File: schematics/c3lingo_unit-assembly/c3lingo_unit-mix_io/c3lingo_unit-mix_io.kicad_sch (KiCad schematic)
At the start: 45 parts, among them J201 Stage Line-In, J202 Mix Line-Out, J203 PowerSupply, J204 Ch1, J205 Ch2, J206 Ch3, SW201 GND Lift, U201 LM833-N, U202 DRV135UA, U203 LM833-N

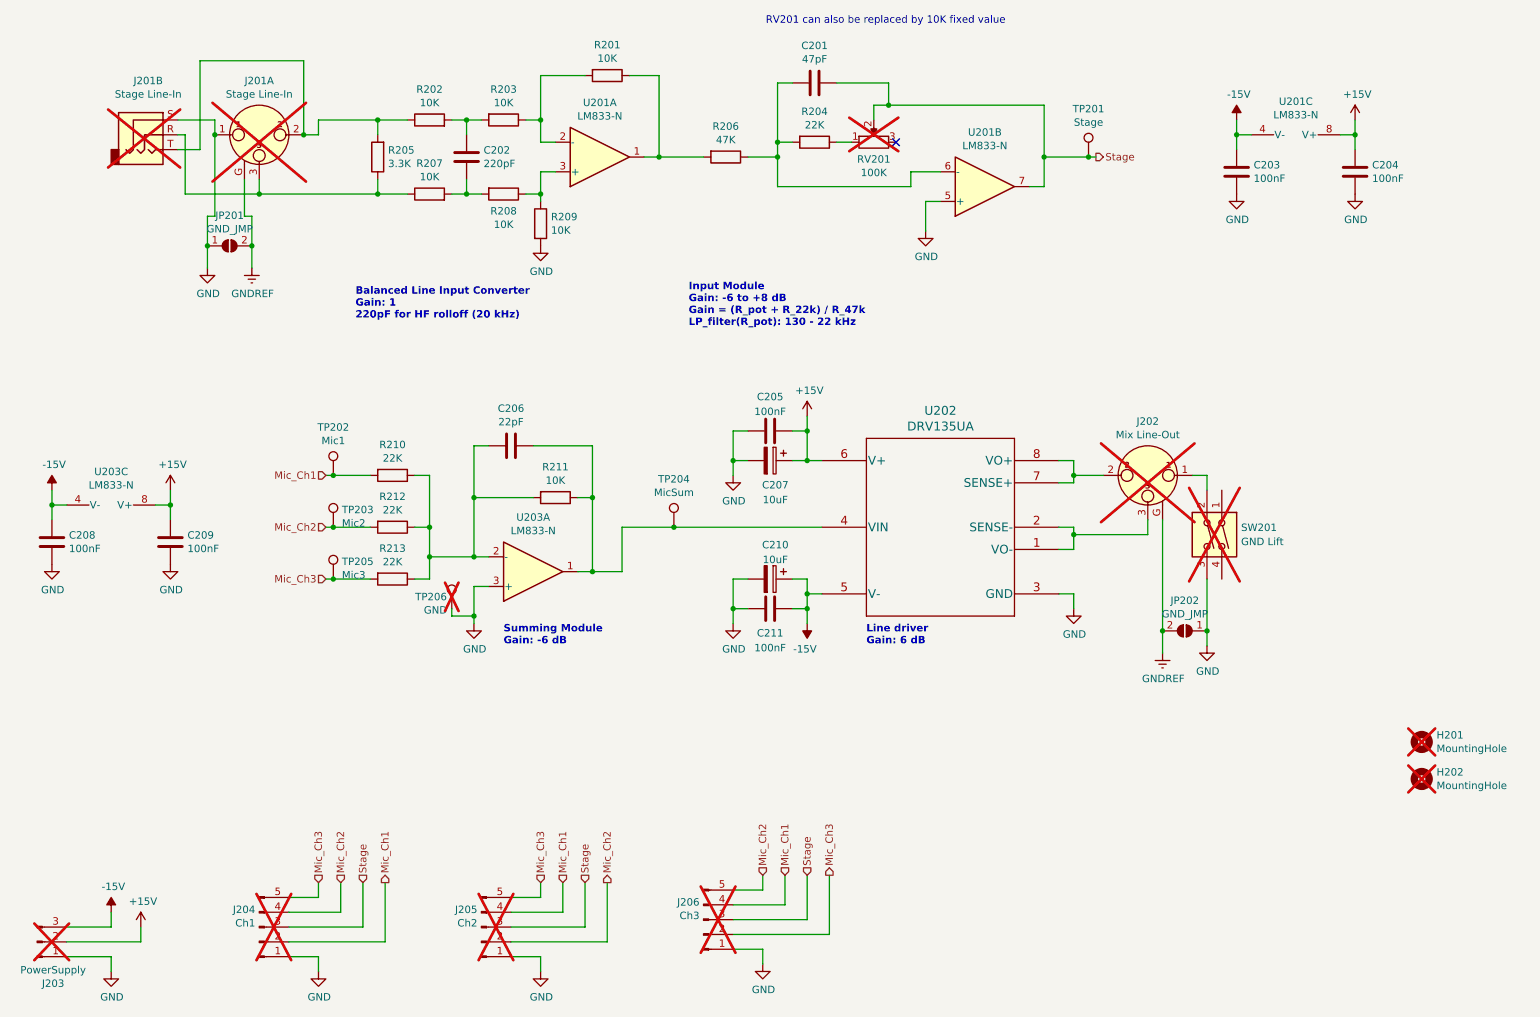
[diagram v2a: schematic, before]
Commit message: Line I/O: Remove gain adjustment (PCB not updated!)
Tweaking the line input gain is not necessary as the users will adjust the volume to personal preference anyways.

Note: PCB not updated!
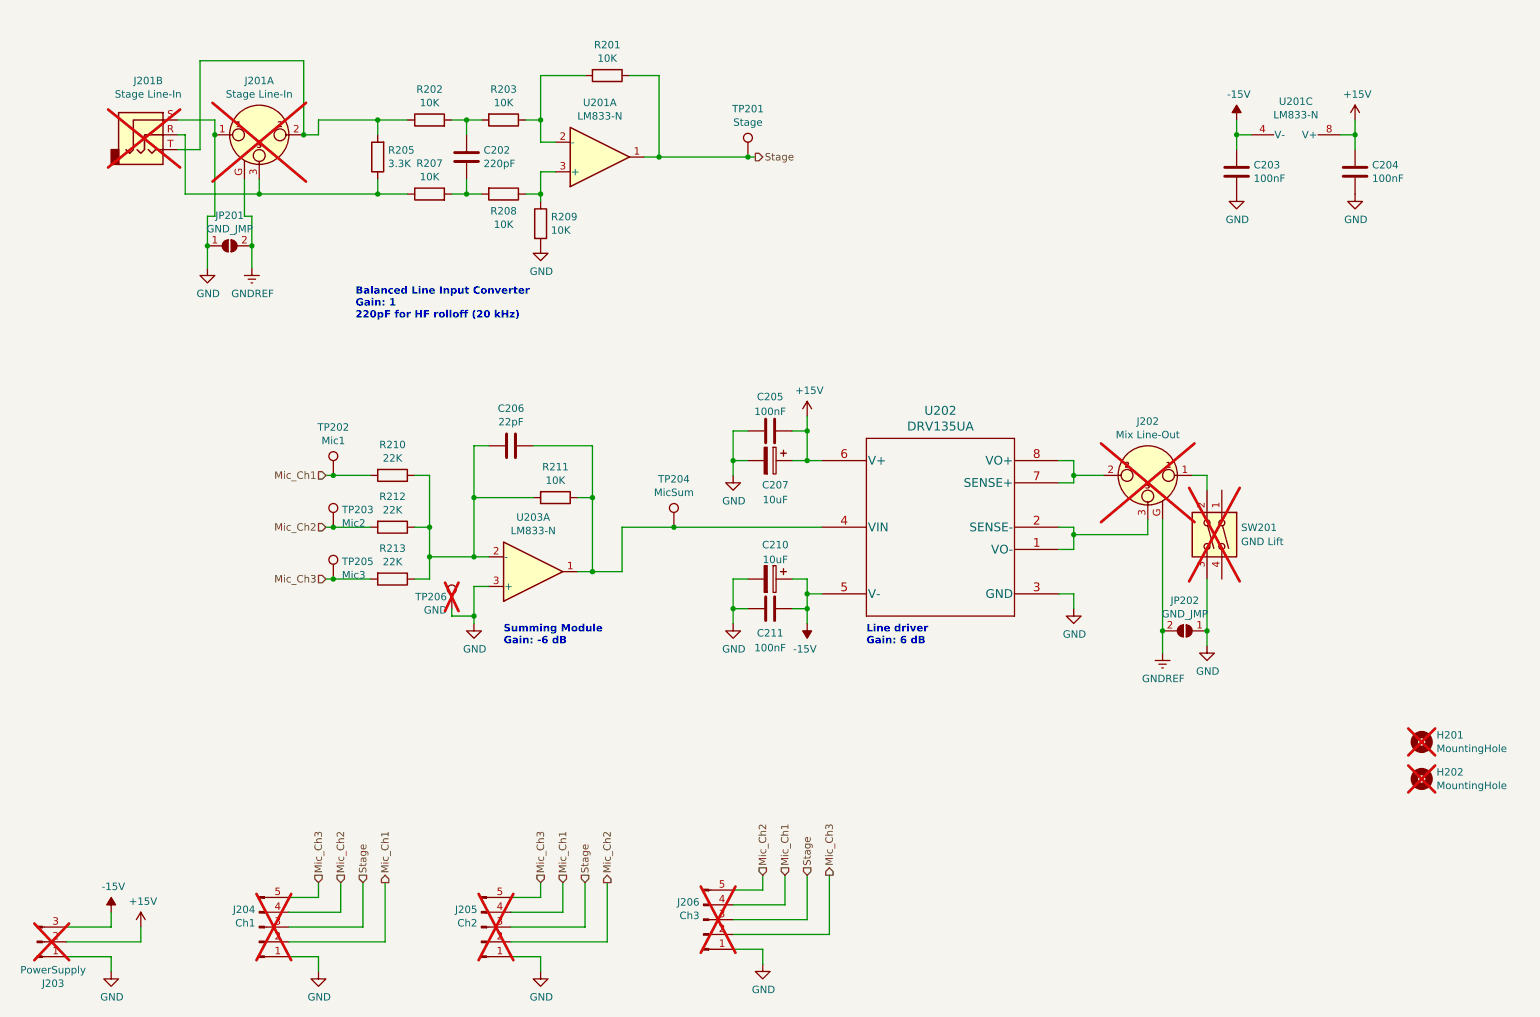
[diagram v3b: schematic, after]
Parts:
- removed C201: 47pF, Capacitor_SMD:C_0603_1608Metric_Pad1.08x0.95mm_HandSolder, symbol Device:C
- removed C208, C209: 100nF, Capacitor_SMD:C_0603_1608Metric_Pad1.08x0.95mm_HandSolder, symbol Device:C
- removed R204: 22K, Resistor_SMD:R_0805_2012Metric_Pad1.20x1.40mm_HandSolder, symbol Device:R
- removed R206: 47K, Resistor_SMD:R_0805_2012Metric_Pad1.20x1.40mm_HandSolder, symbol Device:R
- removed RV201: 100K, Potentiometer_THT:Potentiometer_Vishay_T73XX_Horizontal, symbol Device:R_Potentiometer
- removed unit 2 of U201
- removed unit 3 of U203
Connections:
- net Stage: now also R201.1, U201.1
- no-connect marks 1 -> 0
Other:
- note removed: "Input Module Gain: -6 to +8 dB Gain = (R_pot + R_22k) / R_47k LP_filter(R_pot): 130 - 22 kHz"
- note removed: "RV201 can also be replaced by 10K fixed value"
- moved on the sheet: TP201

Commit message: Update to KiCad 9
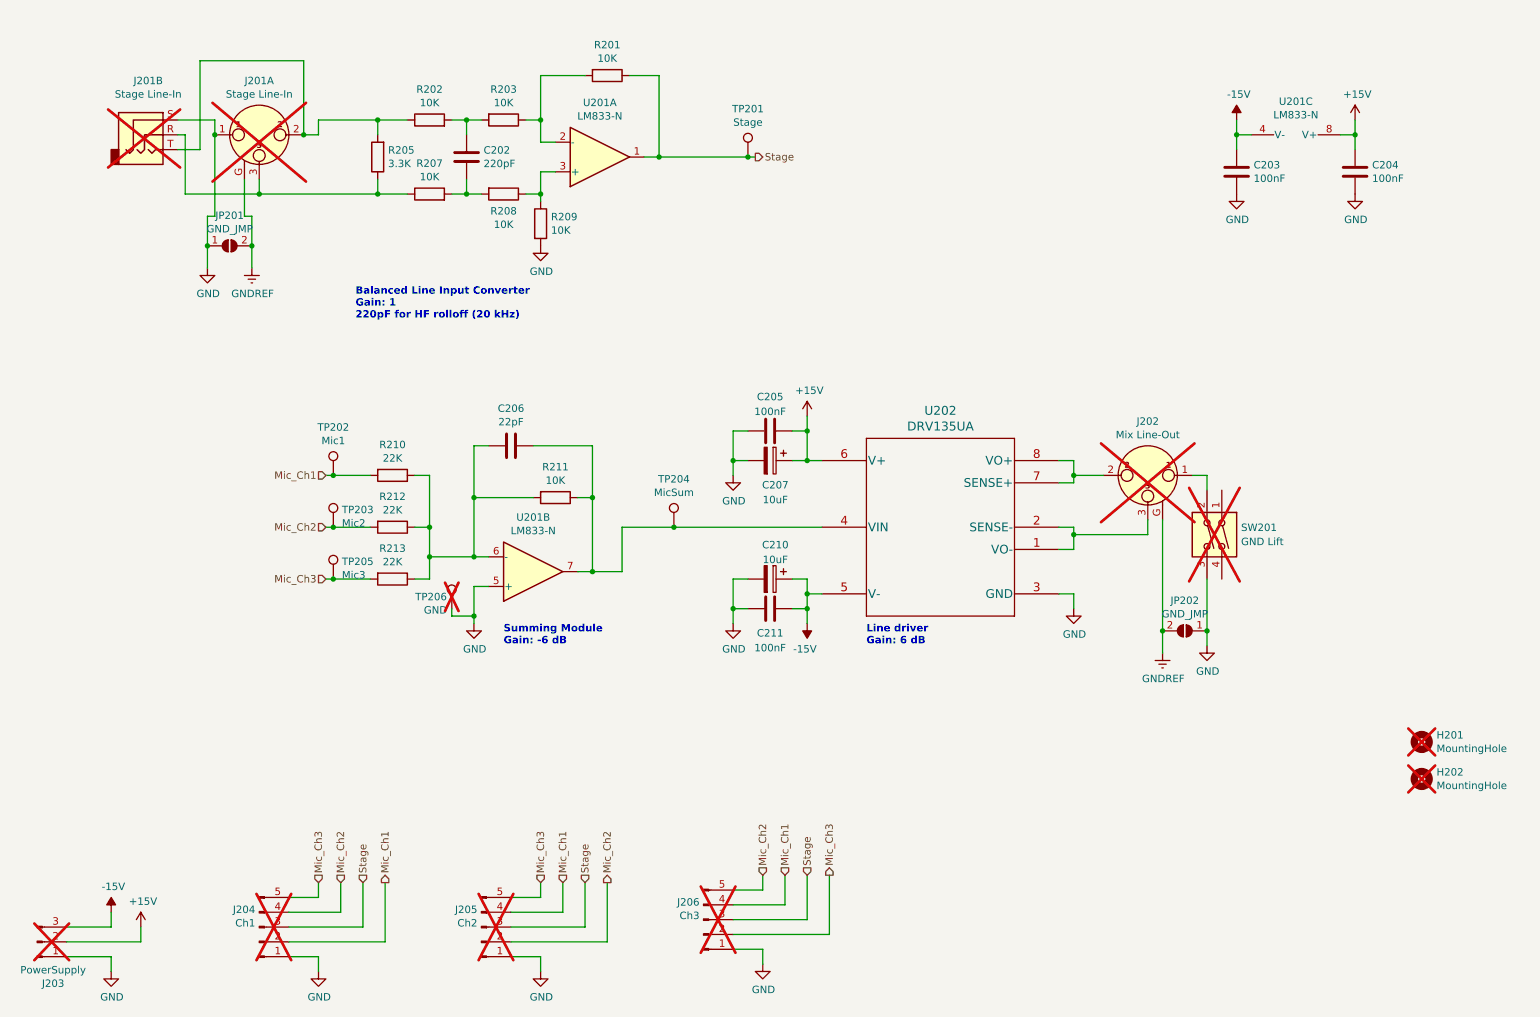
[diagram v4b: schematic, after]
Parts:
- renumbered U203 to U201
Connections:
- net GND: now also U201.5 (+); no longer U201.3 (+)
- net at C206.1, R211.1, TP204.1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: now also U201.7; no longer U201.1
- net at C206.2, R210.1, R211.2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: now also U201.6 (-); no longer U201.2 (-)
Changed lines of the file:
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@@
 (kicad_sch
-	(version 20231120)
+	(version 20250114)
 	(generator "eeschema")
-	(generator_version "8.0")
+	(generator_version "9.0")
 	(paper "A4")
 	(title_block
@@
 		(comment 1 "Prototype 3")
 	)
+	(text "Line driver\nGain: 6 dB"
+		(exclude_from_sim no)
+		(at 167.64 134.62 0)
+		(effects
+			(font
+				(size 1.27 1.27)
+				(thickness 0.254)
+				(bold yes)
+			)
+			(justify left bottom)
+		)
+	)
+	(text "Balanced Line Input Converter\nGain: 1\n220pF for HF rolloff (20 kHz)"
+		(exclude_from_sim no)
+		(at 80.01 78.74 0)
+		(effects
+			(font
+				(size 1.27 1.27)
+				(thickness 0.254)
+				(bold yes)
+			)
+			(justify left bottom)
+		)
+	)
+	(text "Summing Module\nGain: -6 dB"
+		(exclude_from_sim no)
+		(at 105.41 134.62 0)
+		(effects
+			(font
+				(size 1.27 1.27)
+				(thickness 0.254)
+				(bold yes)
+			)
+			(justify left bottom)
+		)
+	)
 	(junction
 		(at 120.65 109.22)
@@
 		)
 	)
-	(text "Line driver\nGain: 6 dB"
-		(exclude_from_sim no)
-		(at 167.64 134.62 0)
-		(effects
-			(font
-				(size 1.27 1.27)
-				(thickness 0.254)
-				(bold yes)
-			)
-			(justify left bottom)
-		)
-	)
-	(text "Balanced Line Input Converter\nGain: 1\n220pF for HF rolloff (20 kHz)"
-		(exclude_from_sim no)
-		(at 80.01 78.74 0)
-		(effects
-			(font
-				(size 1.27 1.27)
-				(thickness 0.254)
-				(bold yes)
-			)
-			(justify left bottom)
-		)
-	)
-	(text "Summing Module\nGain: -6 dB"
-		(exclude_from_sim no)
-		(at 105.41 134.62 0)
-		(effects
-			(font
-				(size 1.27 1.27)
-				(thickness 0.254)
-				(bold yes)
-			)
-			(justify left bottom)
-		)
-	)
 	(hierarchical_label "Mic_Ch1"
 		(shape input)
@@
 		(at 110.49 121.92 0)
 		(mirror x)
-		(unit 1)
+		(unit 2)
 		(exclude_from_sim no)
 		(in_bom yes)
 		(on_board yes)
 		(dnp no)
-		(property "Reference" "U203"
+		(property "Reference" "U201"
 			(at 110.49 112.5982 0)
 			(effects
@@
 		)
 	)
+	(embedded_fonts no)
 )

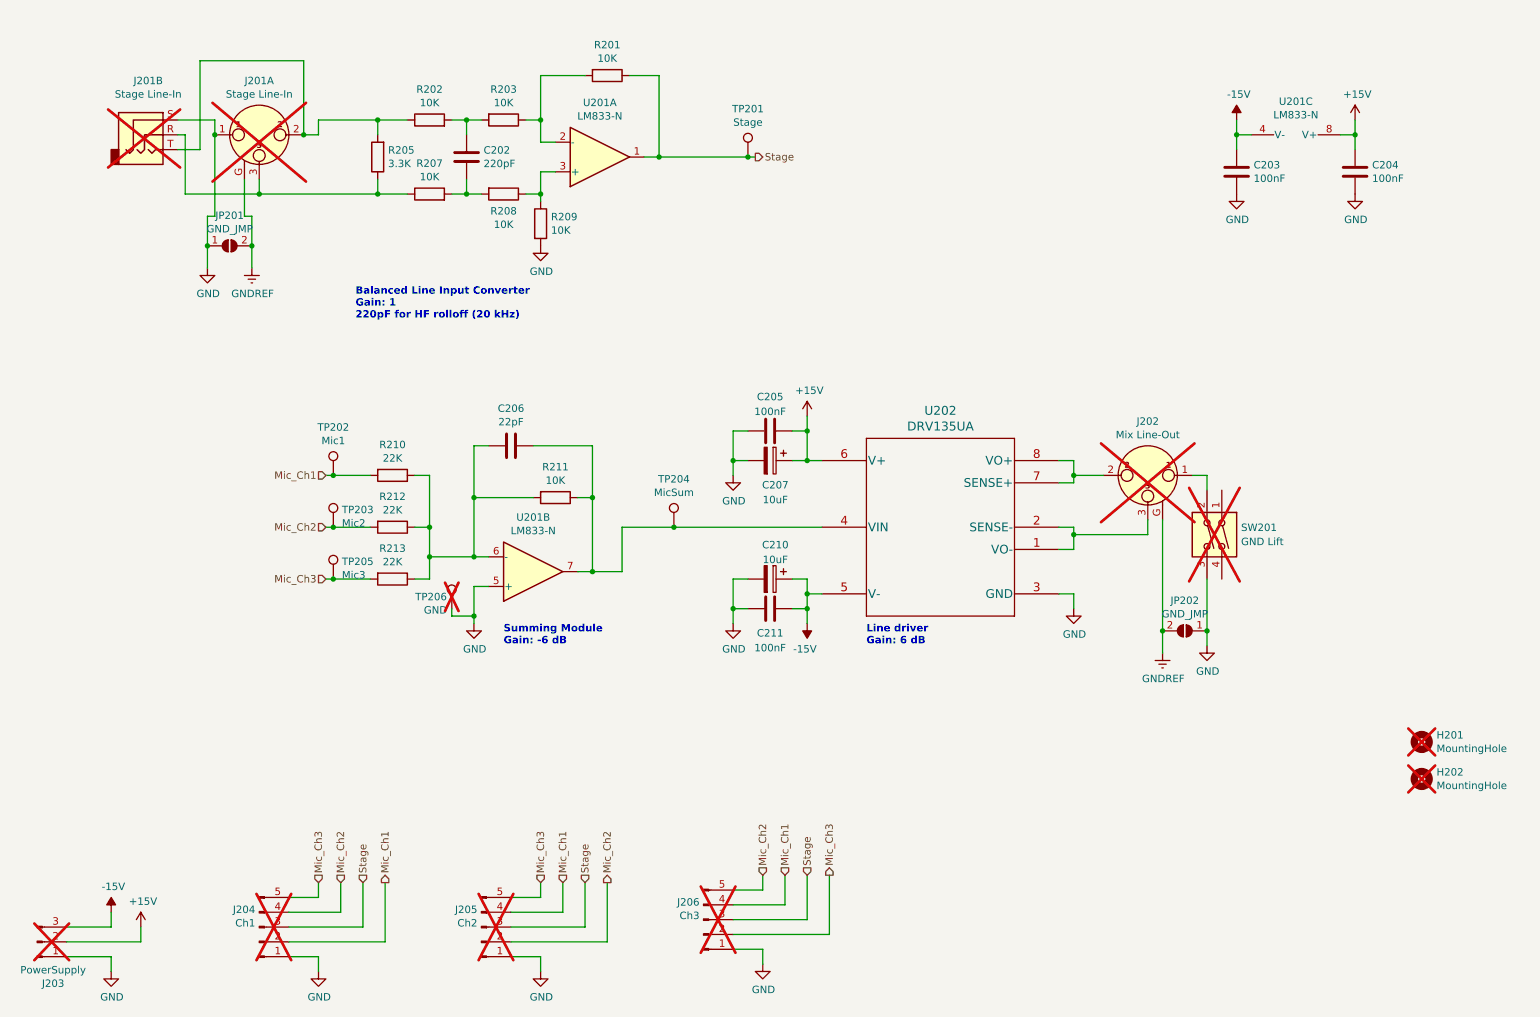
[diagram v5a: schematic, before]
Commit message: Change inter-PCB connections to IDC connectors
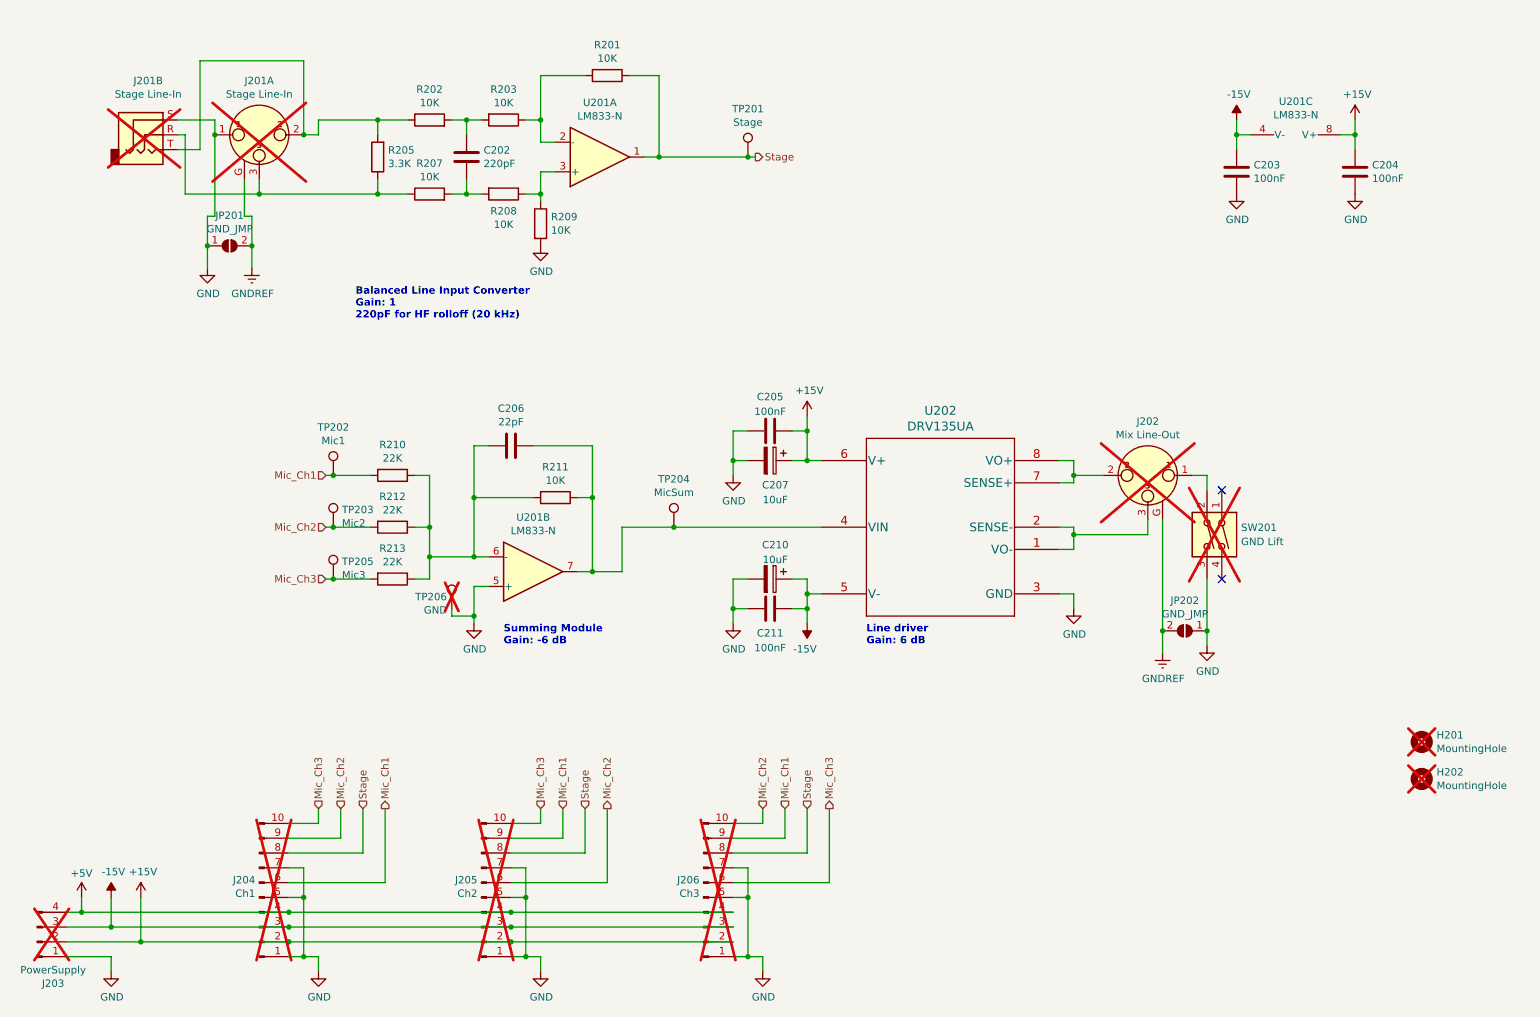
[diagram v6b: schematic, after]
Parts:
- J203: footprint TerminalBlock_Phoenix:TerminalBlock_Phoenix_PTSM-0,5-3-2.5-V-THR_1x03_P2.50mm_Vertical -> c3lingo_unit-footprints:TerminalBlock_Phoenix_SPTAF-1-4-3.5_1x04_P3.5mm; symbol Connector:Conn_01x03_Pin -> Connector:Conn_01x04_Pin; Model PTSM 0,5/ 3-2,5-V THR -> SPTAF 1/ 4-3,5-EL
- J204, J205, J206: footprint TerminalBlock_Phoenix:TerminalBlock_Phoenix_PTSM-0,5-5-2.5-V-THR_1x05_P2.50mm_Vertical -> Connector_IDC:IDC-Header_2x05_P2.54mm_Vertical; symbol Connector:Conn_01x05_Pin -> Connector:Conn_01x10_Pin; Model PTSM 0,5/ 5-2,5-V THR -> Generic IDC Connector
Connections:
- net +15V: now also J204.2 (Pin_2), J205.2 (Pin_2), J206.2 (Pin_2)
- net -15V: now also J204.3 (Pin_3), J205.3 (Pin_3), J206.3 (Pin_3)
- net GND: now also J204.5 (Pin_5), J204.7 (Pin_7), J205.5 (Pin_5), J205.7 (Pin_7), J206.5 (Pin_5), J206.7 (Pin_7)
- net Mic_Ch1: now also J204.6 (Pin_6), J205.9 (Pin_9), J206.9 (Pin_9); no longer J204.2 (Pin_2), J205.4 (Pin_4), J206.4 (Pin_4)
- net Mic_Ch2: now also J204.9 (Pin_9), J205.6 (Pin_6), J206.10 (Pin_10); no longer J204.4 (Pin_4), J205.2 (Pin_2), J206.5 (Pin_5)
- net Mic_Ch3: now also J204.10 (Pin_10), J205.10 (Pin_10), J206.6 (Pin_6); no longer J204.5 (Pin_5), J205.5 (Pin_5), J206.2 (Pin_2)
- net Stage: now also J204.8 (Pin_8), J205.8 (Pin_8), J206.8 (Pin_8); no longer J204.3 (Pin_3), J205.3 (Pin_3), J206.3 (Pin_3)
- new net +5V: J203.4 (Pin_4), J204.4 (Pin_4), J205.4 (Pin_4), J206.4 (Pin_4)
- no-connect marks 0 -> 2

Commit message: Refactor: Rename component rotation
The latest release of the (JLC PCB) Fabrication Toolkit plugin needs the rotation offset field to be named "FT Rotation Offset"
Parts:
- C207, C210: FT Rotation Offset (none) -> 180; JLCPCB Rotation Offset 180 -> (none)
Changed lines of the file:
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@@
 			)
 		)
-		(property "JLCPCB Rotation Offset" "180"
+		(property "FT Rotation Offset" "180"
 			(at 151.13 123.19 90)
 			(effects
@@
 			)
 		)
-		(property "JLCPCB Rotation Offset" "180"
-			(at 151.13 102.87 0)
-			(effects
+		(property "FT Rotation Offset" "180"
+			(at 151.13 102.87 0)
+			(effects
